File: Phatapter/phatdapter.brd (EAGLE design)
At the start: 65 x 78.4 mm, 102 parts, among them J1 RASPBERRYPI-40-PIN-GPIO_SMD_M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, J2 RASPBERRYPI-40-PIN-GPIO_RIGHT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, J3 QWIIC_RIGHT_ANGLE, J5 QWIIC_RIGHT_ANGLE

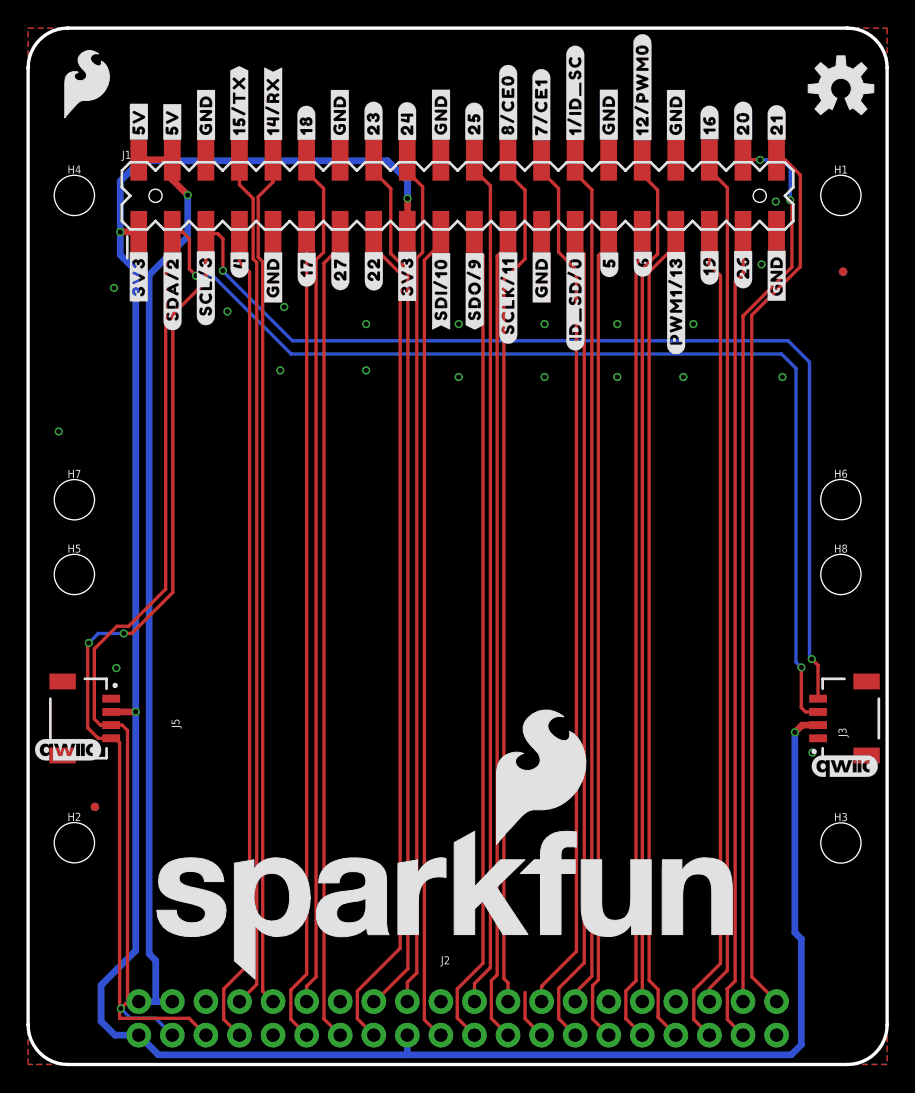
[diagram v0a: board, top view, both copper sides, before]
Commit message: Updates symbol which required an entire reroute of the board
* Adds "qwiic mount" silk
* moves Qwiic connector "lower" on the board to align with standoffs
* Adds standoffs for micro-hats
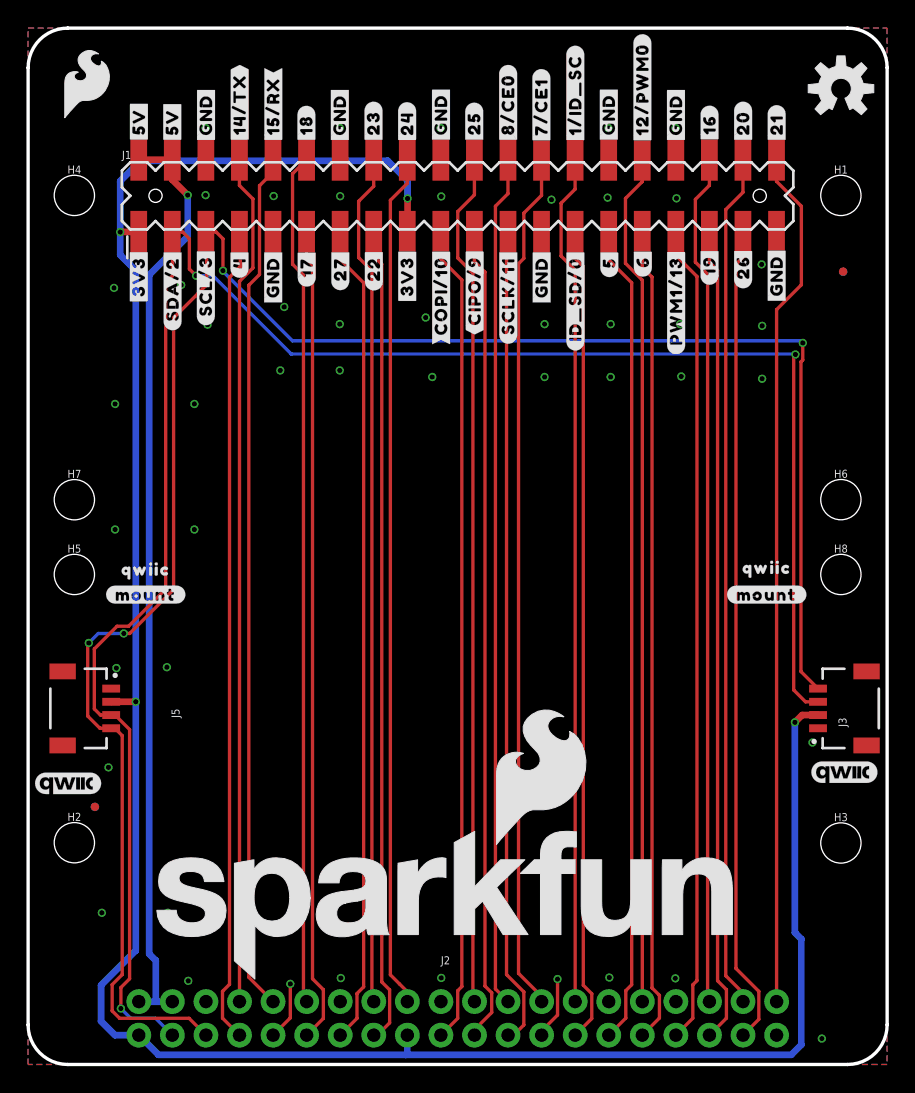
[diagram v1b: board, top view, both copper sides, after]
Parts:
- added U$82, U$83: (no value), top:#MOUNT#29
- added U$84, U$85: (no value), top:QWIIC30
- U$13: device top:#SDO#9#28 -> bot:#10#COPI#28
- U$18: device top:#14#RX#29 -> bot:#RX#15#29
- U$19: device top:#15#TX#29 -> bot:#TX#14#29
- U$3: device top:#SDI#10#28 -> bot:#9#CIPO#28
- U$51: device bot:#9#SDO#28 -> top:#CIPO#9#28
- U$52: device bot:#10#SDI#28 -> top:#COPI#10#28
- U$75: device bot:#RX#14#29 -> top:#14#TX#29
- U$76: device bot:#TX#15#29 -> top:#15#RX#29
- moved U$13 2.59 mm to (31.2, 58.2), flipped to the bottom, turned to 270 degrees
- moved U$76 2.57 mm to (18.5, 72.5), flipped to the top, turned to 90 degrees
- moved U$3 2.54 mm to (33.8, 58.5), flipped to the bottom, turned to 270 degrees
- moved LOGO1 2.54 mm to (2.99, 21.3)
- moved U$75 2.52 mm to (16.0, 72.6), flipped to the top, turned to 90 degrees
- moved J3 0.76 mm to (59.8, 26.9)
- moved J5 0.76 mm to (6.28, 26.9)
- moved U$52 0.51 mm to (31.2, 58.2), flipped to the top, turned to 90 degrees
- moved LOGO4 0.46 mm to (61.7, 22.1)
- moved U$51 0.13 mm to (33.8, 58.5), flipped to the top, turned to 90 degrees
- moved U$19 0.07 mm to (16.0, 72.6), flipped to the bottom, turned to 270 degrees
- flipped U$18 to the bottom, turned to 270 degrees
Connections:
- net GP12 renamed 12/PCM0
- net GP13 renamed 13/PCM1
- net GP18 renamed 18/PCM_CLK
- net GP19 renamed 19/PCM_FS
- net GP20 renamed 20/PCM_DIN
- net GP21 renamed 21/PCM_DOUT
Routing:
- net GND: track 3.75 -> 9.16 mm, vias 20 -> 48
- net 20/PCM_DIN: track 68.5 -> 64.8 mm, vias 2 -> 0
- net 21/PCM_DOUT: track 67.1 -> 65.3 mm
- net GP22: track 63.5 -> 61.9 mm
- net GP23: track 65.9 -> 64.6 mm
- net 3.3V: track 177.0 -> 177.8 mm
- net 7/CE1: track 65.9 -> 65.1 mm
- net 19/PCM_FS: track 62.5 -> 61.8 mm
- net 15/RXI: track 64.6 -> 65.2 mm
- net 0/ID_SD: track 62.4 -> 61.8 mm
- net 8/CE0: track 65.0 -> 64.5 mm
- net 9/CIPO: track 62.4 -> 61.9 mm
- net GP4: track 62.4 -> 61.9 mm

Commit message: Swaps the rows of PTH holes on the right angle connector
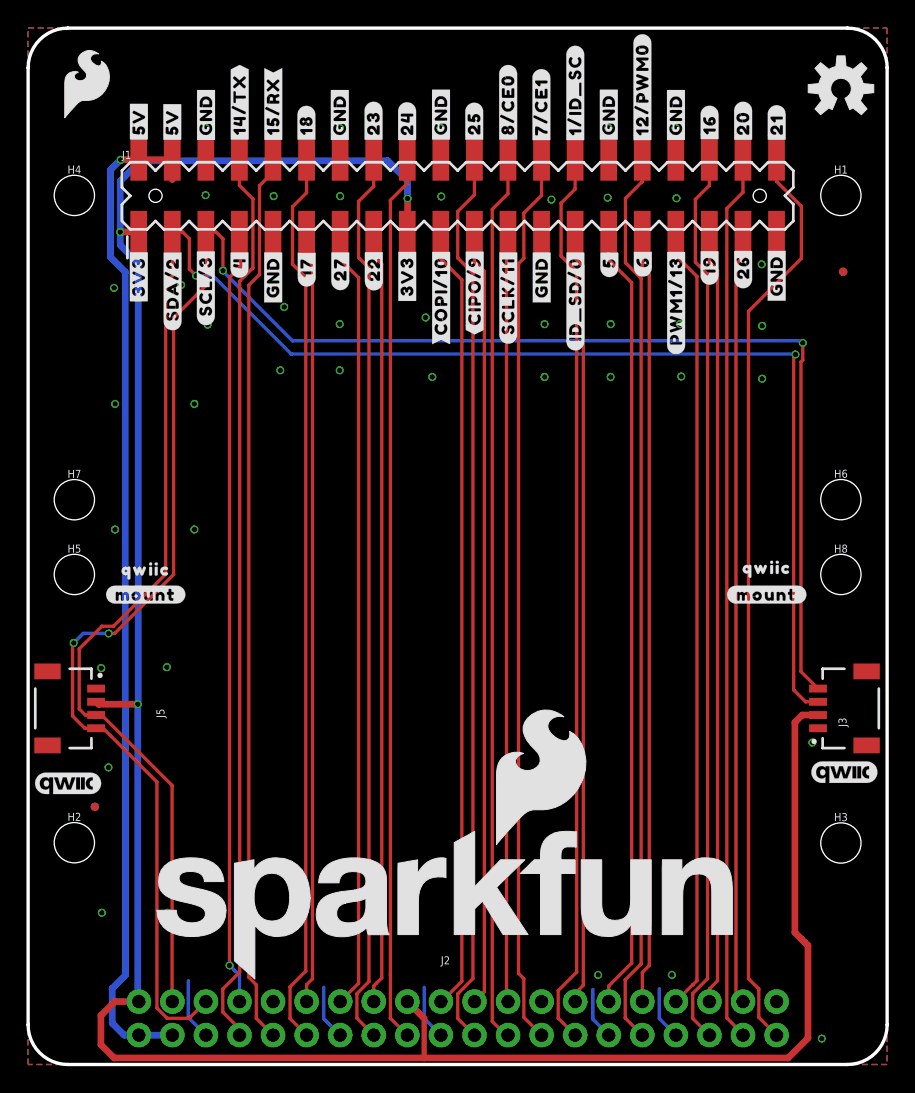
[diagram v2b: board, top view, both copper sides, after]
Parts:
- moved J5 1.14 mm to (5.13, 26.9)
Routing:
- net GND: track 9.16 -> 20.9 mm, vias 48 -> 43
- net 3.3V: track 177.8 -> 185.3 mm, vias 4 -> 3
- net 5V: track 70.7 -> 76.9 mm
- net 21/PCM_DOUT: track 65.3 -> 69.6 mm
- net 11/SCLK: track 62.1 -> 58.3 mm
- net 1/ID_SC: track 64.6 -> 68.3 mm
- net 14/TXO: track 64.5 -> 68.1 mm
- net 12/PCM0: track 64.8 -> 68.3 mm
- net GP26: track 62.2 -> 58.7 mm
- net 18/PCM_CLK: track 64.6 -> 68.1 mm
- net GP25: track 64.7 -> 68.2 mm
- net GP16: track 64.6 -> 68.1 mm
- net GP23: track 64.6 -> 67.9 mm
- net GP17: track 61.8 -> 58.6 mm
- net GP22: track 61.9 -> 58.7 mm
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
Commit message: Adds name to board
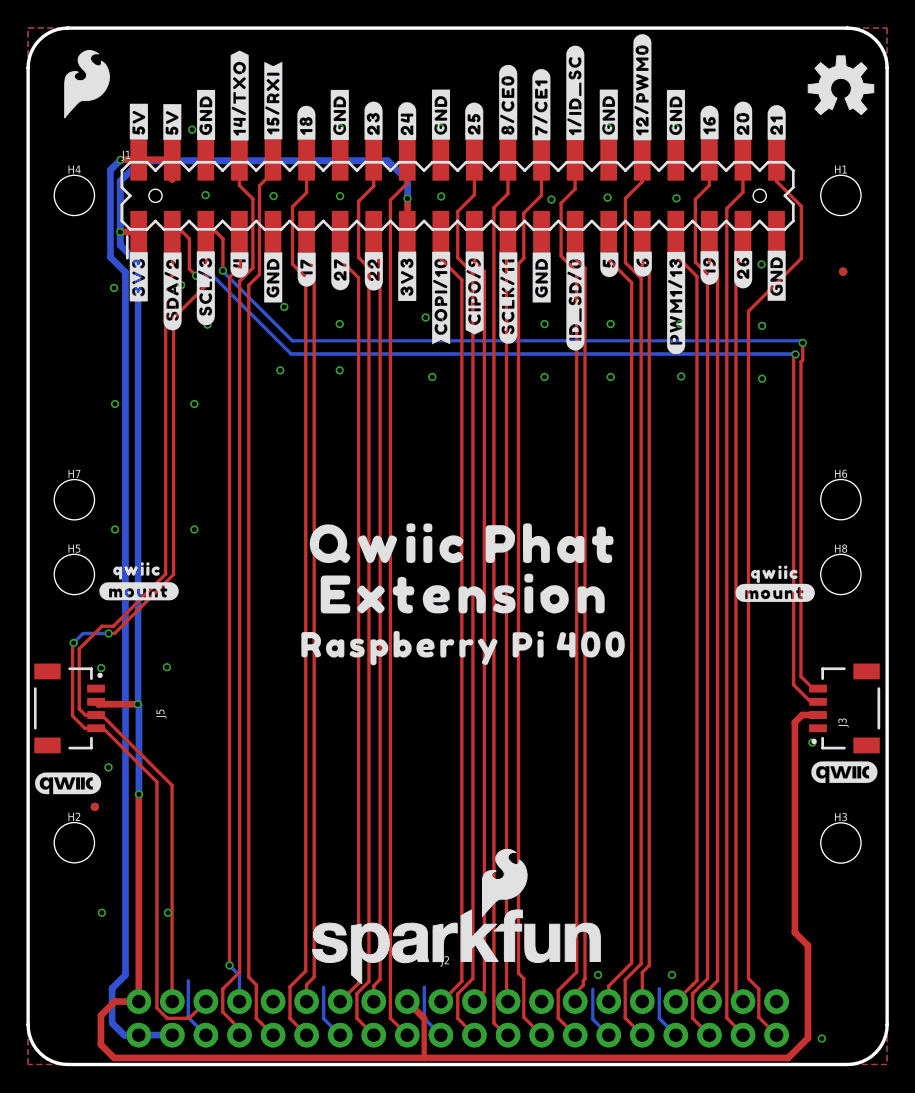
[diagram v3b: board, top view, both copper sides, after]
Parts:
- added LOGO5: SFE_LOGO_NAME_FLAME.2_INCH, SparkFun-Aesthetics:SFE_LOGO_NAME_FLAME_.2
- added U$86, U$91: (no value), top:RASPBERRY_PI_40033
- added U$87: (no value), bot:#RXI#15#29
- added U$88: (no value), bot:#TXO#14#29
- added U$89: (no value), top:QWIIC_PHAT31
- added U$90: (no value), top:EXTENSION32
- LOGO2: value SFE_LOGO_NAME_FLAME.4_INCH -> SFE_LOGO_NAME_FLAME.2_INCH; device SparkFun-Aesthetics:SFE_LOGO_NAME_FLAME_.4 -> SparkFun-Aesthetics:SFE_LOGO_NAME_FLAME_.2
- U$18: device bot:#RX#15#29 -> top:#14#TXO#29
- U$19: device bot:#TX#14#29 -> top:#15#RXI#29
- U$75: device top:#14#TX#29 -> top:QWIIC_PHAT31
- U$76: device top:#15#RX#29 -> top:EXTENSION32
- moved U$76 39.7 mm to (33.0, 35.6), turned to 0 degrees
- moved U$75 37.4 mm to (33.0, 39.4), turned to 0 degrees
- moved LOGO2 23.6 mm to (32.5, 8.93)
- moved U$18 2.62 mm to (16.0, 73.2), flipped to the top, turned to 90 degrees
- moved U$19 2.54 mm to (18.5, 72.8), flipped to the top, turned to 90 degrees
- moved U$85 0.74 mm to (56.5, 37.2)
- moved U$83 0.65 mm to (56.5, 35.7)
- moved U$84 0.63 mm to (8.26, 37.5)
- moved U$82 0.57 mm to (8.38, 35.8)
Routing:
- net 3.3V: track 185.3 -> 185.4 mm, vias 3 -> 4

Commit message: Removes labels from underneath the board
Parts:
- removed U$13: (no value), bot:#10#COPI#28
- removed U$3: (no value), bot:#9#CIPO#28
- removed U$41: (no value), bot:#0#ID_SD#28
- removed U$42: (no value), bot:#2#SDA#4
- removed U$43: (no value), bot:#3#SCL#4
- removed U$44, U$45: (no value), bot:#3V3#0
- removed U$46: (no value), bot:#4#4
- removed U$47: (no value), bot:#5#28
- removed U$48, U$49: (no value), top:#5V#28
- removed U$50: (no value), bot:#6#28
- removed U$53: (no value), bot:#11#SCLK#28
- removed U$54: (no value), bot:#13#PWM1#28
- removed U$55: (no value), bot:#16#29
- removed U$56: (no value), bot:#17#5
- removed U$57: (no value), bot:#18#29
- removed U$58: (no value), bot:#19#28
- removed U$59: (no value), bot:#20#29
- removed U$60: (no value), bot:#21#29
- removed U$61: (no value), bot:#22#28
- removed U$62: (no value), bot:#23#29
- removed U$63: (no value), bot:#24#29
- removed U$64: (no value), bot:#CE1#7#29
- removed U$65, U$66, U$67, U$68, U$69, U$70, U$71, U$72: (no value), bot:#GND#28
- removed U$73: (no value), bot:#ID_SC#1#29
- removed U$74: (no value), bot:#PWM0#12#29
- removed U$77: (no value), bot:#CE0#8#29
- removed U$78: (no value), bot:#25#29
- removed U$79: (no value), bot:#27#18
- removed U$80: (no value), bot:#26#28
- removed U$87: (no value), bot:#RXI#15#29
- removed U$88: (no value), bot:#TXO#14#29
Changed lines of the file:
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@@
 <element name="U$15" library="top" package="#ID_SD#0#28" value="" x="41.402" y="57.912" smashed="yes" rot="R90"/>
 <element name="U$17" library="top" package="#PWM1#13#28" value="" x="49.022" y="57.785" smashed="yes" rot="R90"/>
-<element name="U$41" library="bot" package="#0#ID_SD#28" value="" x="41.402" y="57.912" smashed="yes" rot="MR270"/>
-<element name="U$42" library="bot" package="#2#SDA#4" value="" x="10.922" y="58.674" smashed="yes" rot="MR270"/>
-<element name="U$43" library="bot" package="#3#SCL#4" value="" x="13.441" y="58.9095" smashed="yes" rot="MR270"/>
-<element name="U$44" library="bot" package="#3V3#0" value="" x="8.366" y="59.563" smashed="yes" rot="MR270"/>
-<element name="U$45" library="bot" package="#3V3#0" value="" x="28.6766" y="59.6392" smashed="yes" rot="MR270"/>
-<element name="U$46" library="bot" package="#4#4" value="" x="15.986" y="60.6665" smashed="yes" rot="MR270"/>
-<element name="U$47" library="bot" package="#5#28" value="" x="43.942" y="60.706" smashed="yes" rot="MR270"/>
-<element name="U$48" library="top" package="#5V#28" value="" x="8.3756" y="71.2978" smashed="yes" rot="MR270"/>
-<element name="U$49" library="top" package="#5V#28" value="" x="10.8966" y="71.3232" smashed="yes" rot="MR270"/>
-<element name="U$50" library="bot" package="#6#28" value="" x="46.506" y="60.7315" smashed="yes" rot="MR270"/>
-<element name="U$53" library="bot" package="#11#SCLK#28" value="" x="36.322" y="58.166" smashed="yes" rot="MR270"/>
-<element name="U$54" library="bot" package="#13#PWM1#28" value="" x="49.022" y="57.785" smashed="yes" rot="MR270"/>
-<element name="U$55" library="bot" package="#16#29" value="" x="51.562" y="71.12" smashed="yes" rot="MR270"/>
-<element name="U$56" library="bot" package="#17#5" value="" x="21.082" y="60.325" smashed="yes" rot="MR270"/>
-<element name="U$57" library="bot" package="#18#29" value="" x="21.0566" y="71.0946" smashed="yes" rot="MR270"/>
-<element name="U$58" library="bot" package="#19#28" value="" x="51.562" y="60.452" smashed="yes" rot="MR270"/>
-<element name="U$59" library="bot" package="#20#29" value="" x="54.102" y="71.247" smashed="yes" rot="MR270"/>
-<element name="U$60" library="bot" package="#21#29" value="" x="56.642" y="71.12" smashed="yes" rot="MR270"/>
-<element name="U$61" library="bot" package="#22#28" value="" x="26.162" y="60.198" smashed="yes" rot="MR270"/>
-<element name="U$62" library="bot" package="#23#29" value="" x="26.1366" y="71.247" smashed="yes" rot="MR270"/>
-<element name="U$63" library="bot" package="#24#29" value="" x="28.6766" y="71.2216" smashed="yes" rot="MR270"/>
-<element name="U$64" library="bot" package="#CE1#7#29" value="" x="38.8366" y="72.4662" smashed="yes" rot="MR270"/>
-<element name="U$65" library="bot" package="#GND#28" value="" x="13.462" y="71.8566" smashed="yes" rot="MR270"/>
-<element name="U$66" library="bot" package="#GND#28" value="" x="18.542" y="59.563" smashed="yes" rot="MR270"/>
-<element name="U$67" library="bot" package="#GND#28" value="" x="38.862" y="59.563" smashed="yes" rot="MR270"/>
-<element name="U$68" library="bot" package="#GND#28" value="" x="56.642" y="59.69" smashed="yes" rot="MR270"/>
-<element name="U$69" library="bot" package="#GND#28" value="" x="49.022" y="71.8566" smashed="yes" rot="MR270"/>
-<element name="U$70" library="bot" package="#GND#28" value="" x="43.942" y="71.882" smashed="yes" rot="MR270"/>
-<element name="U$71" library="bot" package="#GND#28" value="" x="31.242" y="71.882" smashed="yes" rot="MR270"/>
-<element name="U$72" library="bot" package="#GND#28" value="" x="23.5789" y="71.8566" smashed="yes" rot="MR270"/>
-<element name="U$73" library="bot" package="#ID_SC#1#29" value="" x="41.402" y="73.3552" smashed="yes" rot="MR270"/>
-<element name="U$74" library="bot" package="#PWM0#12#29" value="" x="46.482" y="73.787" smashed="yes" rot="MR270"/>
-<element name="U$77" library="bot" package="#CE0#8#29" value="" x="36.322" y="72.644" smashed="yes" rot="MR270"/>
-<element name="U$78" library="bot" package="#25#29" value="" x="33.7566" y="71.2216" smashed="yes" rot="MR270"/>
-<element name="U$79" library="bot" package="#27#18" value="" x="23.622" y="60.198" smashed="yes" rot="MR270"/>
-<element name="U$80" library="bot" package="#26#28" value="" x="54.102" y="60.325" smashed="yes" rot="MR270"/>
 <element name="U$81" library="SparkFun-Aesthetics" package="SFE_LOGO_FLAME_.2" value="" x="4.445" y="74.168" smashed="yes"/>
 <element name="H6" library="SparkFun-Hardware" package="STAND-OFF-TIGHT" value="STAND-OFFTIGHT" x="61.49" y="42.746" smashed="yes">
@@
 <attribute name="VALUE" x="61.49" y="35.433" size="0.6096" layer="27" font="vector" ratio="20" align="top-center"/>
 </element>
-<element name="U$3" library="bot" package="#9#CIPO#28" value="" x="33.782" y="58.547" smashed="yes" rot="MR270"/>
-<element name="U$13" library="bot" package="#10#COPI#28" value="" x="31.242" y="58.166" smashed="yes" rot="MR270"/>
 <element name="U$51" library="top" package="#CIPO#9#28" value="" x="33.782" y="58.547" smashed="yes" rot="R90"/>
 <element name="U$52" library="top" package="#COPI#10#28" value="" x="31.242" y="58.166" smashed="yes" rot="R90"/>
@@
 <element name="U$76" library="top" package="EXTENSION32" value="" x="33.02" y="35.56" smashed="yes"/>
 <element name="U$86" library="top" package="RASPBERRY_PI_40033" value="" x="33.02" y="31.75" smashed="yes"/>
-<element name="U$87" library="bot" package="#RXI#15#29" value="" x="18.542" y="72.771" smashed="yes" rot="MR270"/>
-<element name="U$88" library="bot" package="#TXO#14#29" value="" x="16.002" y="73.152" smashed="yes" rot="MR270"/>
 <element name="U$89" library="top" package="QWIIC_PHAT31" value="" x="33.02" y="39.37" smashed="yes" rot="MR0"/>
 <element name="U$90" library="top" package="EXTENSION32" value="" x="33.02" y="35.56" smashed="yes" rot="MR0"/>

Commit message: Adds "for the" silk, shrinks SparkFun logo
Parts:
- added U$13, U$3: (no value), top:FOR_THE40034
- moved U$86 2.54 mm to (33.0, 29.2)
- moved U$91 2.54 mm to (33.0, 29.2)
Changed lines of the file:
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@@
 <element name="U$75" library="top" package="QWIIC_PHAT31" value="" x="33.02" y="39.37" smashed="yes"/>
 <element name="U$76" library="top" package="EXTENSION32" value="" x="33.02" y="35.56" smashed="yes"/>
-<element name="U$86" library="top" package="RASPBERRY_PI_40033" value="" x="33.02" y="31.75" smashed="yes"/>
+<element name="U$86" library="top" package="RASPBERRY_PI_40033" value="" x="33.02" y="29.21" smashed="yes"/>
 <element name="U$89" library="top" package="QWIIC_PHAT31" value="" x="33.02" y="39.37" smashed="yes" rot="MR0"/>
 <element name="U$90" library="top" package="EXTENSION32" value="" x="33.02" y="35.56" smashed="yes" rot="MR0"/>
-<element name="U$91" library="top" package="RASPBERRY_PI_40033" value="" x="33.02" y="31.75" smashed="yes" rot="MR0"/>
+<element name="U$91" library="top" package="RASPBERRY_PI_40033" value="" x="33.02" y="29.21" smashed="yes" rot="MR0"/>
 <element name="LOGO5" library="SparkFun-Aesthetics" package="SFE_LOGO_NAME_FLAME_.2" value="SFE_LOGO_NAME_FLAME.2_INCH" x="32.285" y="8.933" smashed="yes" rot="MR0"/>
+<element name="U$3" library="top" package="FOR_THE40034" value="" x="32.639" y="31.877" smashed="yes"/>
+<element name="U$13" library="top" package="FOR_THE40034" value="" x="32.131" y="31.877" smashed="yes" rot="MR0"/>
 </elements>
 <signals>
